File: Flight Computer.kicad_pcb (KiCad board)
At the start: 2 copper layers, 46 x 78.2 mm, 26 parts, among them J1 BB_6.35mm, J2 Sig_Out, Q1 Q_PMOS, Q2 Q_PMOS, Q3 Q_NMOS_SGD, Q4 Q_NMOS_SGD, U1 BMP280, U2 Teensy3.5, U3 Adafruit_GPS_THT, U5 VXO7803-1000

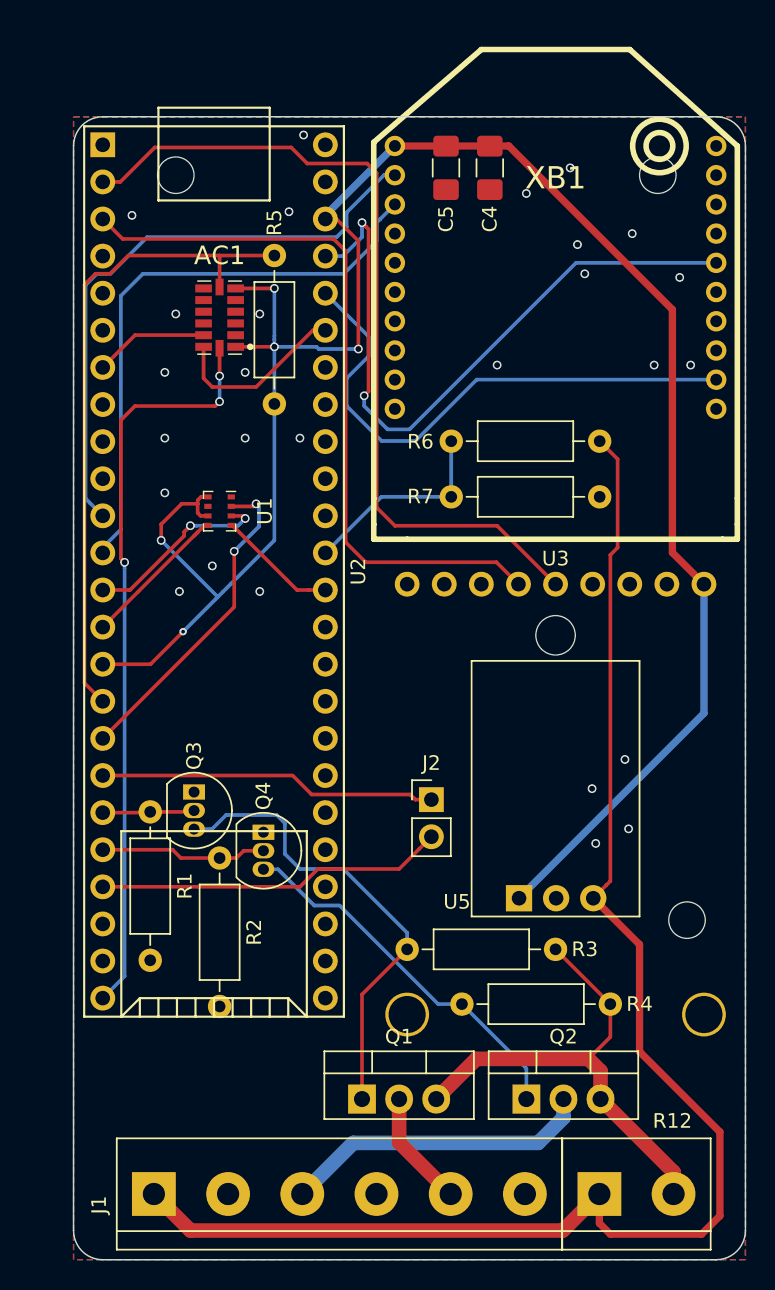
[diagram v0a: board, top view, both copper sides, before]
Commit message: Removed redundant ADC protection diodes Basic PCB component layout
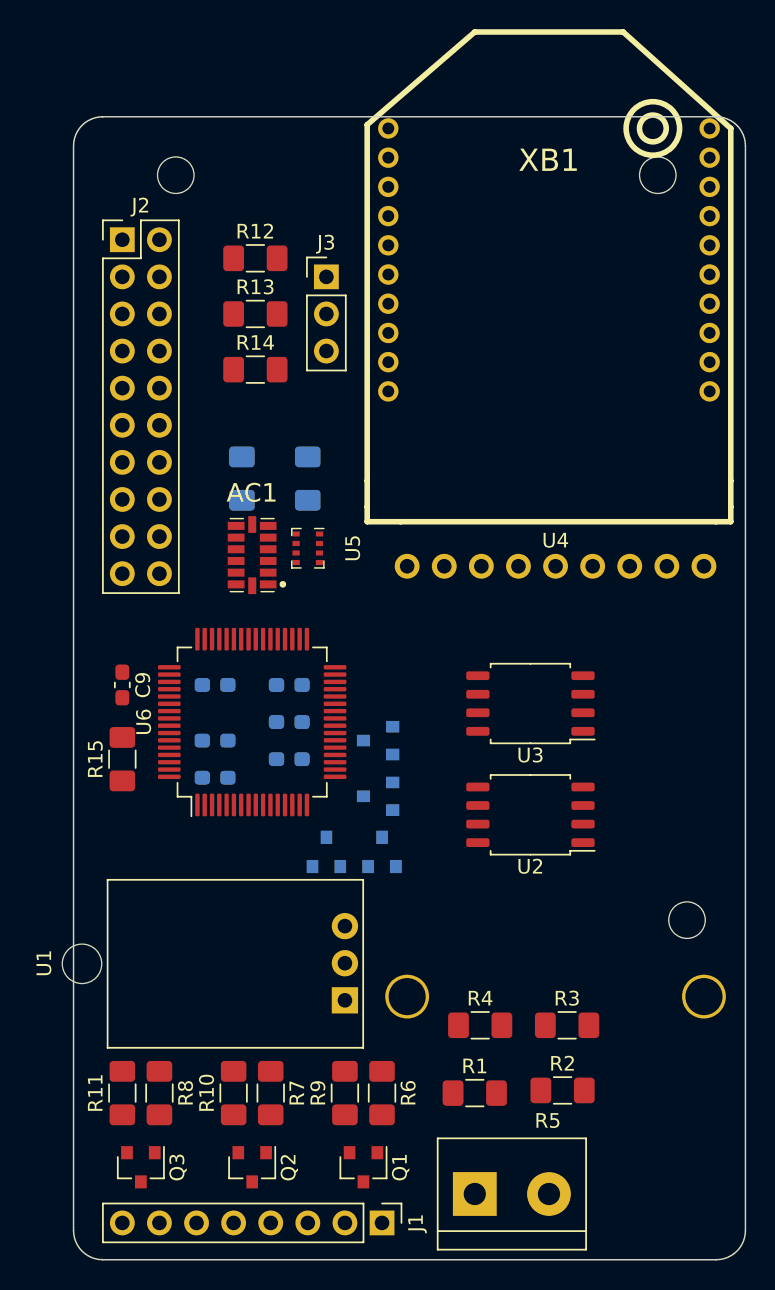
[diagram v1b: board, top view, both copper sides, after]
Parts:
- removed Q4: Q_NMOS_SGD, Package_TO_SOT_THT:TO-92_Inline
- removed the R1 at (55.2, 97.6)
- removed the R2 at (60.0, 100.8)
- removed the R5 at (63.8, 59.5)
- removed the U5 at (80.5, 103.5)
- added C3: 0.1uF, Capacitor_SMD:C_0603_1608Metric_Pad1.05x0.95mm_HandSolder, B.Cu at (64.8, 91.4)
- added C4: 0.1uF, Capacitor_SMD:C_0603_1608Metric_Pad1.05x0.95mm_HandSolder, B.Cu at (64.8, 88.9)
- added C5: 0.1uF, Capacitor_SMD:C_0603_1608Metric_Pad1.05x0.95mm_HandSolder, B.Cu at (64.8, 94.0)
- added C6: 0.1uF, Capacitor_SMD:C_0603_1608Metric_Pad1.05x0.95mm_HandSolder, B.Cu at (59.7, 95.2)
- added C7: 0.1uF, Capacitor_SMD:C_0603_1608Metric_Pad1.05x0.95mm_HandSolder, B.Cu at (59.7, 92.7)
- added C8: 0.1uF, Capacitor_SMD:C_0603_1608Metric_Pad1.05x0.95mm_HandSolder, B.Cu at (59.7, 88.9)
- added C9: 0.1uF, Capacitor_SMD:C_0603_1608Metric_Pad1.05x0.95mm_HandSolder, F.Cu at (53.3, 88.9)
- added D1: BAT54S, Package_TO_SOT_SMD:SOT-23, B.Cu at (67.3, 100.3)
- added D2: BAT54S, Package_TO_SOT_SMD:SOT-23, B.Cu at (71.1, 100.3)
- added D3: BAT54S, Package_TO_SOT_SMD:SOT-23, B.Cu at (70.8, 96.5)
- added D4: BAT54S, Package_TO_SOT_SMD:SOT-23, B.Cu at (70.8, 92.7)
- added J3: BOOT, Connector_PinHeader_2.54mm:PinHeader_1x03_P2.54mm_Vertical, F.Cu at (67.3, 61.0)
- added R11: 10k, Resistor_SMD:R_1206_3216Metric_Pad1.42x1.75mm_HandSolder, F.Cu at (53.3, 116.8)
- added R12: 10k, Resistor_SMD:R_1206_3216Metric_Pad1.42x1.75mm_HandSolder, F.Cu at (62.4, 59.7)
- added R13: 10k, Resistor_SMD:R_1206_3216Metric_Pad1.42x1.75mm_HandSolder, F.Cu at (62.4, 63.5)
- added R14: 10k, Resistor_SMD:R_1206_3216Metric_Pad1.42x1.75mm_HandSolder, F.Cu at (62.4, 67.3)
- added R15: 10k, Resistor_SMD:R_1206_3216Metric_Pad1.42x1.75mm_HandSolder, F.Cu at (53.3, 94.0)
- added R3: 33k, Resistor_SMD:R_1206_3216Metric_Pad1.42x1.75mm_HandSolder, F.Cu at (83.8, 112.2)
- added R4: 10k, Resistor_SMD:R_1206_3216Metric_Pad1.42x1.75mm_HandSolder, F.Cu at (77.8, 112.2)
- added R6: 5.1k, Resistor_SMD:R_1206_3216Metric_Pad1.42x1.75mm_HandSolder, F.Cu at (71.1, 116.8)
- added R7: 5.1k, Resistor_SMD:R_1206_3216Metric_Pad1.42x1.75mm_HandSolder, F.Cu at (63.5, 116.8)
- added R8: 5.1k, Resistor_SMD:R_1206_3216Metric_Pad1.42x1.75mm_HandSolder, F.Cu at (55.9, 116.8)
- added U1: VXO7803-1000, Flight-Computer:VXO7803-1000, F.Cu at (68.6, 110.5)
- added U3: W25Q32JVSS, Package_SO:SOIC-8_5.23x5.23mm_P1.27mm, F.Cu at (81.3, 90.2)
- added U6: STM32F303RETx, Package_QFP:LQFP-64_10x10mm_P0.5mm, F.Cu at (62.2, 91.4)
- C1: renamed from C4; moved to B.Cu
- C2: renamed from C5; moved to B.Cu
- J1: value BB_6.35mm -> Conn_01x08; footprint TerminalBlock:TerminalBlock_bornier-6_P5.08mm -> Connector_PinHeader_2.54mm:PinHeader_1x08_P2.54mm_Vertical
- J2: value Sig_Out -> JTAG; footprint Pin_Headers:Pin_Header_Straight_1x02_Pitch2.54mm -> Connector_PinHeader_2.54mm:PinHeader_2x10_P2.54mm_Vertical
- Q1, Q2: value Q_PMOS -> Q_PMOS_GDS; footprint Package_TO_SOT_THT:TO-220-3_Vertical -> Package_TO_SOT_SMD:SOT-23
- Q3: value Q_NMOS_SGD -> Q_PMOS_GDS; footprint Package_TO_SOT_THT:TO-92_Inline -> Package_TO_SOT_SMD:SOT-23
- R1: renamed from R6; footprint Resistor_THT:R_Axial_DIN0207_L6.3mm_D2.5mm_P10.16mm_Horizontal -> Resistor_SMD:R_1206_3216Metric_Pad1.42x1.75mm_HandSolder
- R10: renamed from R4; footprint Resistor_THT:R_Axial_DIN0207_L6.3mm_D2.5mm_P10.16mm_Horizontal -> Resistor_SMD:R_1206_3216Metric_Pad1.42x1.75mm_HandSolder
- R2: renamed from R7; footprint Resistor_THT:R_Axial_DIN0207_L6.3mm_D2.5mm_P10.16mm_Horizontal -> Resistor_SMD:R_1206_3216Metric_Pad1.42x1.75mm_HandSolder
- R9: renamed from R3; footprint Resistor_THT:R_Axial_DIN0207_L6.3mm_D2.5mm_P10.16mm_Horizontal -> Resistor_SMD:R_1206_3216Metric_Pad1.42x1.75mm_HandSolder
- U2: value Teensy3.5 -> W25Q32JVSS; footprint Flight-Computer:Teensy35_36 -> Package_SO:SOIC-8_5.23x5.23mm_P1.27mm
- moved G1 53.8 mm to (127.0, 88.9), turned to 90 degrees
- moved R1 45.4 mm to (77.5, 116.8), turned to 0 degrees
- moved J2 43.8 mm to (53.3, 58.4)
- moved R2 41.3 mm to (83.5, 116.7)
- moved U2 27.3 mm to (81.3, 97.8), turned to 180 degrees
- moved R10 26.5 mm to (61.0, 116.8), turned to 90 degrees
- moved Q3 25.9 mm to (54.6, 121.9)
- moved C2 25.4 mm to (61.5, 74.8), turned to 270 degrees
- moved C1 24.7 mm to (66.0, 74.8), turned to 270 degrees
- moved Q2 19.3 mm to (62.2, 121.9), turned to 270 degrees
- moved R9 17.5 mm to (68.6, 116.8), turned to 90 degrees
- moved AC1 16.4 mm to (62.2, 80.0)
- moved J1 15.7 mm to (71.1, 125.7), turned to 270 degrees
- moved R5 8.53 mm to (77.5, 123.8)
- moved U5 6.55 mm to (66.0, 79.5)
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- renumbered R12 to R5, U3 to U4, U1 to U5
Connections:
- AC1 pad 10: Net-(AC1-Pad10) -> (no net)
- AC1 pad 11: Net-(AC1-Pad11) -> (no net)
- AC1 pad 12: /ADXL_MISO -> /SPI1_MISO
- AC1 pad 13: /ADXL_MOSI -> /SPI1_MOSI
- AC1 pad 14: /ADXL_SCLK -> /SPI1_SCK
- AC1 pad 3: Net-(AC1-Pad3) -> (no net)
- AC1 pad 7: /ADXL_CS -> /SPI1_CS1
- AC1 pad 8: Net-(AC1-Pad8) -> (no net)
- AC1 pad 9: Net-(AC1-Pad9) -> (no net)
- J1 pad 3: /MAIN_POW -> /DROGUE_POW
- J1 pad 5: /DROGUE_POW -> /MAIN_POW
- J2 pad 1: /LAUNCHED -> +3V3
- J2 pad 2: /LANDED -> +3V3
- Q1 pad 2: /DROGUE_POW -> Net-(Q1-Pad2)
- Q1 pad 3: Net-(Q1-Pad3) -> /DROGUE_POW
- Q2 pad 2: /MAIN_POW -> Net-(Q1-Pad2)
- Q2 pad 3: Net-(Q1-Pad3) -> /MAIN_POW
- Q3 pad 1: GND -> Net-(Q3-Pad1)
- Q3 pad 2: /DROGE_IGN -> Net-(Q1-Pad2)
- Q3 pad 3: Net-(Q1-Pad1) -> /AUX1_POW
- R1 pad 2: /BAT_V_DIV -> /ADC1
- R10 pad 1: Net-(Q1-Pad3) -> Net-(Q1-Pad2)
- R2 pad 1: /BAT_V_DIV -> /ADC1
- R5 pad 2: Net-(Q1-Pad3) -> Net-(Q1-Pad2)
- R9 pad 1: Net-(Q1-Pad3) -> Net-(Q1-Pad2)
- U2 pad 1: GND -> /SPI2_CS1
- U2 pad 2: /GPS_TX -> /SPI2_MISO
- U2 pad 3: /GPS_RX -> (no net)
- U2 pad 4: Net-(U2-Pad4) -> GND
- U2 pad 5: Net-(U2-Pad5) -> /SPI2_MOSI
- U2 pad 6: Net-(U2-Pad6) -> /SPI2_SCK
- U2 pad 7: /ADXL_MISO -> (no net)
- U2 pad 8: Net-(U2-Pad8) -> +3V3
- U4 pad 2: Net-(U3-Pad2) -> (no net)
- U4 pad 3: Net-(U3-Pad3) -> (no net)
- U4 pad 4: Net-(U3-Pad4) -> (no net)
- U4 pad 5: /GPS_TX -> /USART2_TX
- U4 pad 6: /GPS_RX -> /USART2_RX
- U4 pad 8: Net-(U3-Pad8) -> (no net)
- U4 pad 9: Net-(U3-Pad9) -> (no net)
- U5 pad 2: /BMP_CS -> /SPI1_CS2
- U5 pad 3: /BMP_MOSI -> /SPI1_MOSI
- U5 pad 4: /BMP_SCLK -> /SPI1_SCK
- U5 pad 5: /BMP_MISO -> /SPI1_MISO
- XB1 pad 11: Net-(XB1-Pad11) -> (no net)
- XB1 pad 12: /XBEE_CTS -> (no net)
- XB1 pad 13: Net-(XB1-Pad13) -> (no net)
- XB1 pad 14: Net-(XB1-Pad14) -> (no net)
- XB1 pad 15: Net-(XB1-Pad15) -> (no net)
- XB1 pad 16: /XBEE_RTS -> (no net)
- XB1 pad 17: Net-(XB1-Pad17) -> (no net)
- XB1 pad 18: Net-(XB1-Pad18) -> (no net)
- XB1 pad 19: Net-(XB1-Pad19) -> (no net)
- XB1 pad 2: /XBEE_TX -> /USART1_RX
- XB1 pad 20: Net-(XB1-Pad20) -> (no net)
- XB1 pad 3: /XBEE_RX -> /USART1_TX
- XB1 pad 4: Net-(XB1-Pad4) -> (no net)
- XB1 pad 5: Net-(XB1-Pad5) -> (no net)
- XB1 pad 6: Net-(XB1-Pad6) -> (no net)
- XB1 pad 7: Net-(XB1-Pad7) -> (no net)
- XB1 pad 8: Net-(XB1-Pad8) -> (no net)
- XB1 pad 9: Net-(XB1-Pad9) -> (no net)
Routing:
- net +3V3: track 143.1 -> 0.00 mm, vias 5 -> 0
- net +BATT: track 101.5 -> 0.00 mm
- net /GPS_TX: track 57.8 -> 0.00 mm
- net /ADXL_SCLK: track 51.2 -> 0.00 mm, vias 3 -> 0
- net /GPS_RX: track 50.5 -> 0.00 mm
- net /XBEE_RTS: track 46.4 -> 0.00 mm, vias 2 -> 0
- net /ADXL_CS: track 45.3 -> 0.00 mm
- net /XBEE_TX: track 41.4 -> 0.00 mm
- net /XBEE_RX: track 40.2 -> 0.00 mm
- net /XBEE_CTS: track 37.6 -> 0.00 mm
- net Net-(Q1-Pad3): track 32.9 -> 0.00 mm
- net Net-(Q1-Pad1): track 32.4 -> 0.00 mm
- net Net-(Q2-Pad1): track 25.7 -> 0.00 mm
- net /LANDED: track 23.9 -> 0.00 mm
- net /LAUNCHED: track 23.2 -> 0.00 mm
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- added copper zone on In1.Cu, net +3V3
- added copper zone on In2.Cu, net GND
- removed copper zone on B.Cu, net GND
- removed copper zone on F.Cu, net GND
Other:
- copper layers 2 -> 4

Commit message: Fixed .gitmodules (host-agnostic) Added bypass caps Added NMOS to ignition sheet Added current-limiting resistors Fixed 3V3 ADC input
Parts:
- moved R5 2.23 mm to (76.2, 121.9)
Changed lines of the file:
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@@
     (add_net /ACT2)
     (add_net /ACT3)
-    (add_net /ACT4)
     (add_net /ADC1)
     (add_net /ADC2)
@@
     (add_net /AUX1_POW)
     (add_net /DROGUE_POW)
-    (add_net /I2C1_SCL)
-    (add_net /I2C1_SDA)
     (add_net /MAIN_POW)
     (add_net /MCU/JTDI)
@@
     (add_net /SPI1_CS1)
     (add_net /SPI1_CS2)
-    (add_net /SPI1_CS3)
-    (add_net /SPI1_CS4)
     (add_net /SPI1_MISO)
     (add_net /SPI1_MOSI)
@@
     (add_net /USART2_TX)
     (add_net GND)
-    (add_net "Net-(AC1-Pad10)")
-    (add_net "Net-(AC1-Pad11)")
-    (add_net "Net-(AC1-Pad3)")
-    (add_net "Net-(AC1-Pad8)")
-    (add_net "Net-(AC1-Pad9)")
     (add_net "Net-(J2-Pad11)")
     (add_net "Net-(J2-Pad17)")
@@
     (add_net "Net-(Q2-Pad1)")
     (add_net "Net-(Q3-Pad1)")
-    (add_net "Net-(U2-Pad3)")
-    (add_net "Net-(U2-Pad7)")
-    (add_net "Net-(U3-Pad3)")
-    (add_net "Net-(U3-Pad7)")
-    (add_net "Net-(U4-Pad2)")
-    (add_net "Net-(U4-Pad3)")
-    (add_net "Net-(U4-Pad4)")
-    (add_net "Net-(U4-Pad8)")
-    (add_net "Net-(U4-Pad9)")
-    (add_net "Net-(U6-Pad2)")
-    (add_net "Net-(U6-Pad20)")
-    (add_net "Net-(U6-Pad24)")
-    (add_net "Net-(U6-Pad25)")
-    (add_net "Net-(U6-Pad26)")
-    (add_net "Net-(U6-Pad27)")
-    (add_net "Net-(U6-Pad28)")
-    (add_net "Net-(U6-Pad29)")
-    (add_net "Net-(U6-Pad3)")
-    (add_net "Net-(U6-Pad37)")
-    (add_net "Net-(U6-Pad38)")
-    (add_net "Net-(U6-Pad39)")
-    (add_net "Net-(U6-Pad4)")
-    (add_net "Net-(U6-Pad40)")
-    (add_net "Net-(U6-Pad45)")
-    (add_net "Net-(U6-Pad5)")
-    (add_net "Net-(U6-Pad51)")
-    (add_net "Net-(U6-Pad52)")
-    (add_net "Net-(U6-Pad53)")
-    (add_net "Net-(U6-Pad54)")
-    (add_net "Net-(U6-Pad57)")
-    (add_net "Net-(U6-Pad6)")
-    (add_net "Net-(XB1-Pad11)")
-    (add_net "Net-(XB1-Pad12)")
-    (add_net "Net-(XB1-Pad13)")
-    (add_net "Net-(XB1-Pad14)")
-    (add_net "Net-(XB1-Pad15)")
-    (add_net "Net-(XB1-Pad16)")
-    (add_net "Net-(XB1-Pad17)")
-    (add_net "Net-(XB1-Pad18)")
-    (add_net "Net-(XB1-Pad19)")
-    (add_net "Net-(XB1-Pad20)")
-    (add_net "Net-(XB1-Pad4)")
-    (add_net "Net-(XB1-Pad5)")
-    (add_net "Net-(XB1-Pad6)")
-    (add_net "Net-(XB1-Pad7)")
-    (add_net "Net-(XB1-Pad8)")
-    (add_net "Net-(XB1-Pad9)")
   )
   (module Flight-Computer:XBEE_PRO_PTH (layer F.Cu)
@@
   )
   (module TerminalBlock:TerminalBlock_bornier-2_P5.08mm (layer F.Cu)
-    (at 77.47 123.75)
+    (at 76.2 121.92)
     (descr "simple 2-pin terminal block, pitch 5.08mm, revamped version of bornier2")
     (tags "terminal block bornier2")

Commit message: Annotated schematic Added 2N7002 packages Updated PCB
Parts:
- removed J3: BOOT, Connector_PinHeader_2.54mm:PinHeader_1x03_P2.54mm_Vertical
- added C10: 10uF, Capacitor_SMD:C_1206_3216Metric_Pad1.42x1.75mm_HandSolder, F.Cu at (80.0, 35.6)
- added C11: 0.1uF, Capacitor_SMD:C_0603_1608Metric_Pad1.05x0.95mm_HandSolder, F.Cu at (79.2, 38.5)
- added C12: 0.1uF, Capacitor_SMD:C_0603_1608Metric_Pad1.05x0.95mm_HandSolder, F.Cu at (85.2, 35.2)
- added C13: 0.1uF, Capacitor_SMD:C_0603_1608Metric_Pad1.05x0.95mm_HandSolder, F.Cu at (83.6, 38.5)
- added C14: 0.1uF, Capacitor_SMD:C_0603_1608Metric_Pad1.05x0.95mm_HandSolder, F.Cu at (87.9, 37.7)
- added C15: 0.1uF, Capacitor_SMD:C_0603_1608Metric_Pad1.05x0.95mm_HandSolder, F.Cu at (87.9, 40.2)
- added C16: 0.1uF, Capacitor_SMD:C_0603_1608Metric_Pad1.05x0.95mm_HandSolder, F.Cu at (70.5, 25.8)
- added D5: RED, LED_SMD:LED_0603_1608Metric_Pad1.05x0.95mm_HandSolder, F.Cu at (66.1, 29.1)
- added D6: YELLOW, LED_SMD:LED_0603_1608Metric_Pad1.05x0.95mm_HandSolder, F.Cu at (66.1, 26.5)
- added D7: GREEN, LED_SMD:LED_0603_1608Metric_Pad1.05x0.95mm_HandSolder, F.Cu at (61.7, 31.5)
- added D8: GREEN, LED_SMD:LED_0603_1608Metric_Pad1.05x0.95mm_HandSolder, F.Cu at (68.3, 23.2)
- added F1: 3A Polyfuse, Fuse:Fuse_1206_3216Metric_Pad1.42x1.75mm_HandSolder, F.Cu at (80.0, 23.6)
- added Q4: Q_NMOS_GDS, Package_TO_SOT_SMD:SOT-23, F.Cu at (79.3, 27.5)
- added Q5: Q_PMOS_GDS, Package_TO_SOT_SMD:SOT-23, F.Cu at (85.2, 24.2)
- added Q6: Q_PMOS_GDS, Package_TO_SOT_SMD:SOT-23, F.Cu at (89.7, 24.2)
- added R16: 1k, Resistor_SMD:R_1206_3216Metric_Pad1.42x1.75mm_HandSolder, F.Cu at (56.5, 31.5)
- added R17: 1k, Resistor_SMD:R_1206_3216Metric_Pad1.42x1.75mm_HandSolder, F.Cu at (63.1, 23.6)
- added R18: 10k, Resistor_SMD:R_1206_3216Metric_Pad1.42x1.75mm_HandSolder, F.Cu at (56.5, 28.2)
- added SW1: Reset, Button_Switch_SMD:SW_Push_1P1T_NO_CK_KMR2, F.Cu at (56.8, 24.3)
- added U7: MAX7375AXR805, Package_TO_SOT_SMD:SOT-323_SC-70, F.Cu at (61.7, 28.4)
- C1: footprint Capacitor_SMD:C_1206_3216Metric_Pad1.42x1.75mm_HandSolder -> Capacitor_SMD:C_0603_1608Metric_Pad1.05x0.95mm_HandSolder
- C2: value 47pF -> 10uF
- J2: footprint Connector_PinHeader_2.54mm:PinHeader_2x10_P2.54mm_Vertical -> Connector_PinHeader_1.27mm:PinHeader_2x04_P1.27mm_Vertical_SMD
- Q2, Q3: value Q_PMOS_GDS -> Q_NMOS_GDS
- R14, R15: value 10k -> 1k
- R3: value 33k -> 100R
- R4: value 10k -> 100R
- R5: value 10 -> 100R; footprint TerminalBlock:TerminalBlock_bornier-2_P5.08mm -> Resistor_SMD:R_1206_3216Metric_Pad1.42x1.75mm_HandSolder
- R6, R7: value 5.1k -> 100R
- R8: value 5.1k -> 10k
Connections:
- C2 pad 2: +3V3 -> +BATT
- J2 pad 2: +3V3 -> /MCU/SWDIO_JTCK
- J2 pad 4: GND -> /USART2_TX
- J2 pad 6: GND -> /MCU/NRST
- J2 pad 7: /MCU/SWDIO_JTMS -> GND
- J2 pad 8: GND -> /MCU/SWDIO_JTMS
- Q1 pad 2: Net-(Q1-Pad2) -> Net-(F1-Pad2)
- Q2 pad 2: Net-(Q1-Pad2) -> Net-(Q1-Pad1)
- Q2 pad 3: /MAIN_POW -> GND
- Q3 pad 2: Net-(Q1-Pad2) -> Net-(Q3-Pad2)
- Q3 pad 3: /AUX1_POW -> GND
- R1 pad 2: /ADC1 -> Net-(R1-Pad2)
- R10 pad 1: Net-(Q1-Pad2) -> Net-(Q3-Pad1)
- R10 pad 2: Net-(Q2-Pad1) -> GND
- R11 pad 1: Net-(Q1-Pad2) -> Net-(Q4-Pad1)
- R11 pad 2: Net-(Q3-Pad1) -> GND
- R12 pad 1: Net-(J2-Pad11) -> Net-(F1-Pad2)
- R12 pad 2: GND -> Net-(Q3-Pad2)
- R13 pad 1: Net-(J2-Pad17) -> Net-(F1-Pad2)
- R13 pad 2: GND -> Net-(Q4-Pad2)
- R14 pad 1: Net-(J2-Pad19) -> Net-(R14-Pad1)
- R14 pad 2: GND -> Net-(D5-Pad2)
- R15 pad 1: +3V3 -> Net-(R15-Pad1)
- R15 pad 2: /MCU/NRST -> Net-(D6-Pad2)
- R2 pad 1: /ADC1 -> Net-(R1-Pad2)
- R3 pad 1: +BATT -> /ADC2
- R3 pad 2: /ADC2 -> +3V3
- R4 pad 1: /ADC2 -> /ADC1
- R4 pad 2: GND -> Net-(R1-Pad2)
- R5 pad 1: +BATT -> /ACT2
- R5 pad 2: Net-(Q1-Pad2) -> Net-(Q3-Pad1)
- R6 pad 2: Net-(Q1-Pad1) -> Net-(Q2-Pad1)
- R7 pad 1: /ACT2 -> /ACT3
- R7 pad 2: Net-(Q2-Pad1) -> Net-(Q4-Pad1)
- R8 pad 1: /ACT3 -> Net-(Q2-Pad1)
- R8 pad 2: Net-(Q3-Pad1) -> GND
- R9 pad 1: Net-(Q1-Pad2) -> Net-(F1-Pad2)
- U6 pad 24: (no net) -> Net-(R14-Pad1)
- U6 pad 25: (no net) -> Net-(R15-Pad1)
- U6 pad 37: (no net) -> Net-(R16-Pad1)
- U6 pad 38: (no net) -> Net-(R17-Pad1)
- U6 pad 5: (no net) -> Net-(U6-Pad5)

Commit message: Finished adding test points Schematic annotated
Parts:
- removed AC1: ADXL345, SamacSys_Parts:CC-14-1
- removed C14: 0.1uF, Capacitor_SMD:C_0603_1608Metric_Pad1.05x0.95mm_HandSolder
- removed D3, D4: BAT54S, Package_TO_SOT_SMD:SOT-23
- added D9: WHITE, LED_SMD:LED_0603_1608Metric_Pad1.05x0.95mm_HandSolder, F.Cu at (133.3, 35.6)
- added R19: 1k, Resistor_SMD:R_1206_3216Metric_Pad1.42x1.75mm_HandSolder, F.Cu at (134.1, 32.6)
- added TP1: +BATT, TestPoint:TestPoint_Pad_D1.0mm, F.Cu at (145.8, 32.5)
- added TP10: ACT4, TestPoint:TestPoint_Pad_D1.0mm, F.Cu at (112.7, 32.5)
- added TP11: BOOT0, TestPoint:TestPoint_Pad_D1.0mm, F.Cu at (106.6, 41.6)
- added TP12: SPI2_CS1, TestPoint:TestPoint_Pad_D1.0mm, F.Cu at (109.6, 38.6)
- added TP13: SPI2_CS2, TestPoint:TestPoint_Pad_D1.0mm, F.Cu at (112.7, 35.5)
- added TP14: SPI2_SCK, TestPoint:TestPoint_Pad_D1.0mm, F.Cu at (115.7, 32.5)
- added TP15: SPI2_MISO, TestPoint:TestPoint_Pad_D1.0mm, F.Cu at (109.6, 41.6)
- added TP16: SPI2_MOSI, TestPoint:TestPoint_Pad_D1.0mm, F.Cu at (106.6, 32.5)
- added TP17: USART1_RX, TestPoint:TestPoint_Pad_D1.0mm, F.Cu at (112.7, 38.6)
- added TP18: SPI1_CS1, TestPoint:TestPoint_Pad_D1.0mm, F.Cu at (115.7, 35.5)
- added TP19: USART1_TX, TestPoint:TestPoint_Pad_D1.0mm, F.Cu at (118.8, 32.5)
- added TP2: ADC1, TestPoint:TestPoint_Pad_D1.0mm, F.Cu at (142.8, 32.5)
- added TP20: SPI1_CS2, TestPoint:TestPoint_Pad_D1.0mm, F.Cu at (112.7, 41.6)
- added TP21: USART2_RX, TestPoint:TestPoint_Pad_D1.0mm, F.Cu at (115.7, 38.6)
- added TP22: SPI1_SCK, TestPoint:TestPoint_Pad_D1.0mm, F.Cu at (118.8, 35.5)
- added TP23: USART2_TX, TestPoint:TestPoint_Pad_D1.0mm, F.Cu at (121.8, 32.5)
- added TP24: SPI1_MISO, TestPoint:TestPoint_Pad_D1.0mm, F.Cu at (115.7, 41.6)
- added TP25: I2C1_SDA, TestPoint:TestPoint_Pad_D1.0mm, F.Cu at (118.8, 38.6)
- added TP26: I2C1_SCL, TestPoint:TestPoint_Pad_D1.0mm, F.Cu at (121.8, 35.5)
- added TP27: SPI1_MOSI, TestPoint:TestPoint_Pad_D1.0mm, F.Cu at (124.9, 32.5)
- added TP3: ADC2, TestPoint:TestPoint_Pad_D1.0mm, F.Cu at (140.1, 36.1)
- added TP4: GND, TestPoint:TestPoint_Pad_D1.0mm, F.Cu at (137.0, 36.1)
- added TP5: 3V3, TestPoint:TestPoint_Pad_D1.0mm, F.Cu at (132.7, 38.4)
- added TP6: OSC_IN, TestPoint:TestPoint_Pad_D1.0mm, F.Cu at (106.6, 35.5)
- added TP7: ACT1, TestPoint:TestPoint_Pad_D1.0mm, F.Cu at (109.6, 32.5)
- added TP8: ACT2, TestPoint:TestPoint_Pad_D1.0mm, F.Cu at (106.6, 38.6)
- added TP9: ACT3, TestPoint:TestPoint_Pad_D1.0mm, F.Cu at (109.6, 35.5)
- added U8: BMP280, Package_LGA:Bosch_LGA-8_2x2.5mm_P0.65mm_ClockwisePinNumbering, F.Cu at (139.2, 32.8)
- J2: footprint Connector_PinHeader_1.27mm:PinHeader_2x04_P1.27mm_Vertical_SMD -> Connector_PinHeader_1.27mm:PinHeader_2x05_P1.27mm_Vertical_SMD
- U2, U3: value W25Q32JVSS -> W25Q16JVSS
- U5: value BMP280 -> ADXL345; footprint Package_LGA:Bosch_LGA-8_2x2.5mm_P0.65mm_ClockwisePinNumbering -> SamacSys_Parts:CC-14-1
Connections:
- net Net-(U6-Pad5) renamed /MCU/OSC_IN
- J2 pad 3: /USART2_RX -> /MCU/NRST
- J2 pad 4: /USART2_TX -> /MCU/SWDIO_JTMS
- J2 pad 5: /MCU/JTDI -> /MCU/USART3_TX
- J2 pad 6: /MCU/NRST -> /USART2_TX
- J2 pad 7: GND -> /MCU/USART3_RX
- J2 pad 8: /MCU/SWDIO_JTMS -> /MCU/JTDI
- U4 pad 1: +3V3 -> (no net)
- U4 pad 8: (no net) -> +3V3
- U4 pad 9: (no net) -> Net-(R19-Pad1)
- U5 pad 1: GND -> +3V3
- U5 pad 2: /SPI1_CS2 -> GND
- U5 pad 3: /SPI1_MOSI -> (no net)
- U5 pad 4: /SPI1_SCK -> GND
- U5 pad 5: /SPI1_MISO -> GND
- U5 pad 7: GND -> /SPI1_CS1
- U5 pad 8: +3V3 -> (no net)
- U6 pad 11: (no net) -> /ACT4
- U6 pad 16: /ADC3 -> (no net)
- U6 pad 17: /ADC4 -> (no net)
- U6 pad 51: (no net) -> /MCU/USART3_TX
- U6 pad 52: (no net) -> /MCU/USART3_RX
- U6 pad 61: (no net) -> /MCU/I2C1_SDA
- U6 pad 62: (no net) -> /MCU/I2C1_SCL
